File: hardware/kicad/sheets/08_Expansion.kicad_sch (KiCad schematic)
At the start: 0 parts

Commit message: Implement Package 09R expansion interface
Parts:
- added C1: 100 nF X7R ±10% local buffer decoupling, symbol IPC100:C
- added C2: 10 µF X7R accessory-bias reservoir; within ICD-00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, symbol IPC100:C
- added C3: 100 nF X7R ±10% core-side buffer decoupling, symbol IPC100:C
- added D1: J10 SDA low-capacitance TVS provision; IEC 61000-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, symbol IPC100:ESD_PROVISION
- added D2: J10 SCL low-capacitance TVS provision; IEC 61000-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, symbol IPC100:ESD_PROVISION
- added D3: EXPANSION_VCC local ESD/reverse-injection provisi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, symbol IPC100:ESD_PROVISION
- added FB1: Accessory-bias filter bead — impedance/current ra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, symbol IPC100:FERRITE
- added R1: 100 kΩ ±1% segment-enable fail-low bias, symbol IPC100:R
- added R2: 4.70 kΩ ±1% J10 SDA pull-up; Sheet 08 external-se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, symbol IPC100:R
- added R3: 4.70 kΩ ±1% J10 SCL pull-up; Sheet 08 external-se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, symbol IPC100:R
- added R4: 47 Ω J10 SDA series damping; final 33–100 Ω by SI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, symbol IPC100:R
- added R5: 47 Ω J10 SCL series damping; final 33–100 Ω by SI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, symbol IPC100:R
- added TP1: EXPANSION_VCC DFT, symbol IPC100:TEST_NODE
- added TP2: SEGMENT_ENABLE DFT, symbol IPC100:TEST_NODE
- added TP3: INTERNAL SDA DFT, symbol IPC100:TEST_NODE
- added TP4: INTERNAL SCL DFT, symbol IPC100:TEST_NODE
- added TP5: J10 SDA DFT, symbol IPC100:TEST_NODE
- added TP6: J10 SCL DFT, symbol IPC100:TEST_NODE
- added U1: 2.9 V assert / 2.7 V deassert rail qualifier; ≥5 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, symbol IPC100:EXPANSION_RAIL_QUALIFIER
- added U2: Dual-supply I2C hot-swap buffer; 100 kHz; fail-di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, symbol IPC100:I2C_SEGMENT_BUFFER
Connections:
- net +3V3_CORE: now also C3.2, U1.3 (GND)
- net EXPANSION_VCC: now also D3.1 (LINE), FB1.1 (IN), TP1.1 (NODE)
- net I2C_SCL: now also TP4.1 (NODE), U2.3 (SCL_INT)
- net I2C_SDA: now also TP3.1 (NODE)
- net J10_I2C_SCL: now also D2.1 (LINE), R5.1, TP6.1 (NODE)
- net J10_I2C_SDA: now also D1.1 (LINE), R4.1, TP5.1 (NODE)
- new net EXPANSION_SEGMENT_ENABLE: R1.2, TP2.1 (NODE), U1.4 (SEGMENT_ENABLE)
- new net EXPANSION_VCC_FILT: C1.2, C2.2, FB1.2 (OUT), R2.2, R3.2, U1.2 (EXP_VCC_SENSE), U2.8 (GND)
- new net EXP_SCL_BUFFERED: R3.1, R5.2, U2.7 (SCL_EXT)
- new net EXP_SDA_BUFFERED: R2.1, R4.2
- new net GND: C1.1, C2.1, C3.1, D1.2 (RETURN), D2.2 (RETURN), D3.2 (RETURN), R1.1, U1.1 (CORE_VDD), U2.5 (VCC_EXT)
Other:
- note added: "1 — OPTIONAL EXPANSION POWER FILTER / RAIL-VALID QUALIFICATION"
- note added: "2 — FAIL-DISABLED SEGMENTED I2C BUFFER (100 kHz; NO CLOCK STRETCHING)"
- note added: "3 — EXTERNAL-SIDE PULL-UPS, SERIES DAMPING & PROTECTION PROVISIONS"
- note added: "4 — SCHEMATIC DFT NODES (PHYSICAL PADS REMAIN SHEET 09 / PCB SCOPE)"
- note added: "Dual-supply hot-swap class: high-Z when disabled/unpowered, ≤10 µA powered-off leakage per line, no false-low startup pulse, external stuck-low isolated after disable. Sheet 07 remains sole internal pull-up owner."
- note added: "ICD-001 REV A RESTRICTIONS: DNP DEFAULT; ONE ACCESSORY; 0x30–0x37; NO CLOCK STRETCHING; NO CAN/RS-485/UART/SPI/USB/RANGEHUB; NO GPIO37; NON-SAFETY FIRMWARE DATA ONLY."
- note added: "One accessory, address 0x30–0x37, 0.30 m maximum, 100 pF segment maximum. Generic TVS provisions require final low-capacitance part/placement selection with Sheet 09; no connector or footprint is present."
- note added: "Probe power, rail-valid enable, both internal bus lines, and both isolated external lines. No footprint assignments are authorized."
- note added: "Sheet 02 remains sole switch/current-limit owner. Sheet 08 filters only its local external-side bias/logic supply and releases the segment at ≥2.9 V after 5 ms; disables by ≤2.7 V. Entire option DNP by default."
- note removed: "Detailed implementation intentionally deferred to subsequent engineering package."
- note removed: "PACKAGE 01 PLACEHOLDER — NO CIRCUITRY OR FOOTPRINTS"
- title: IPC-100 Rev A — 08 Expansion -> IPC-100 Rev A — 08 Restricted Expansion Interface

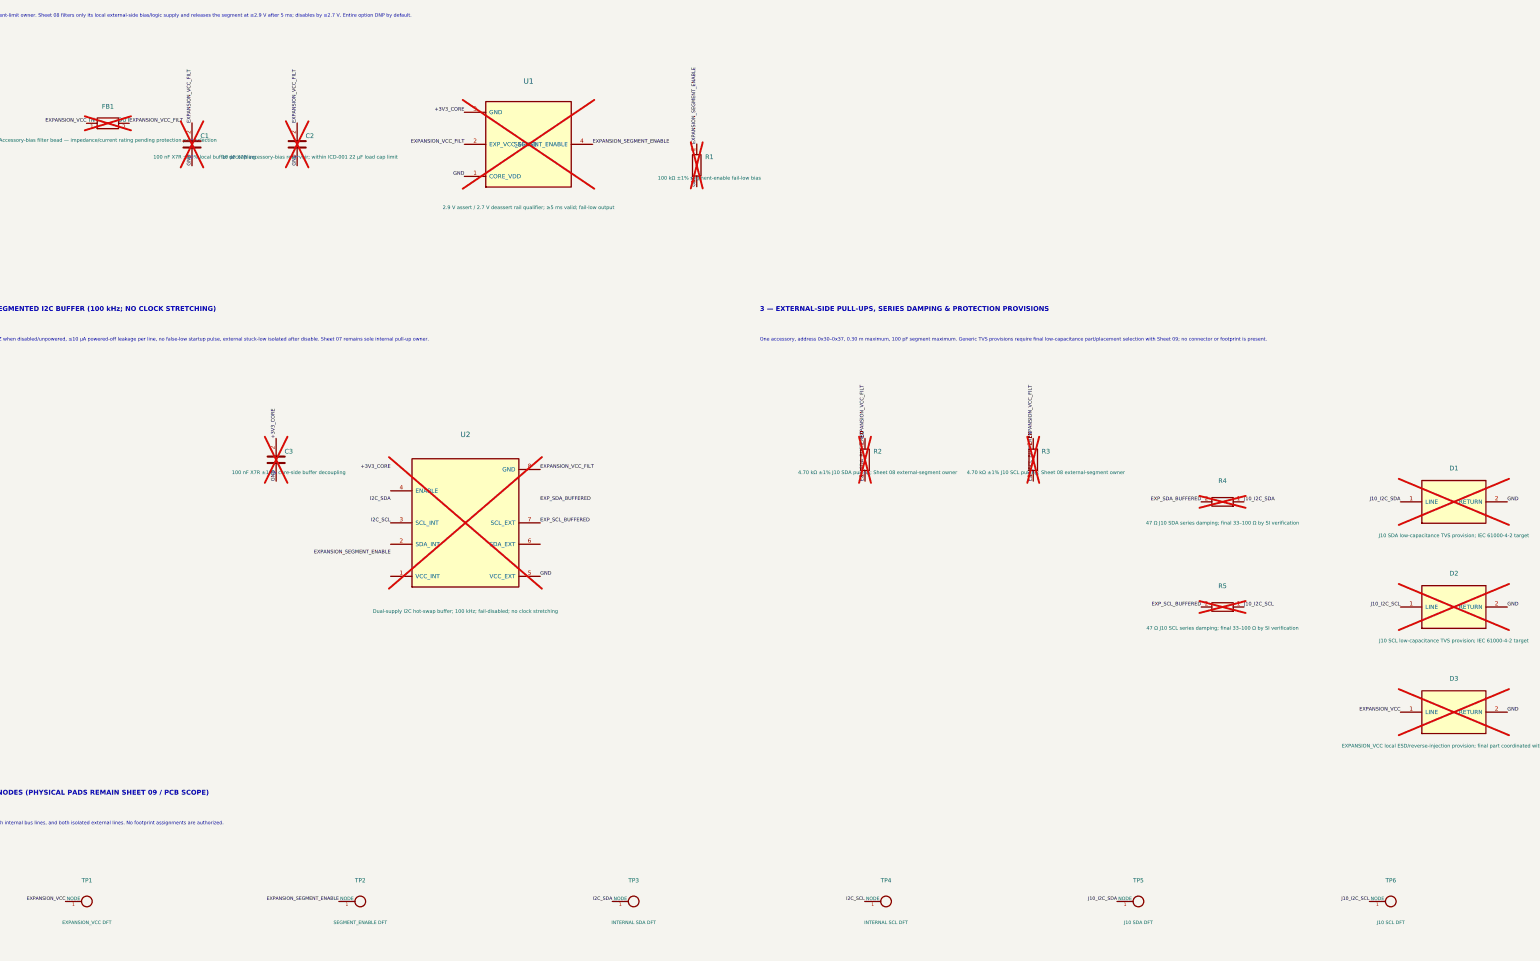
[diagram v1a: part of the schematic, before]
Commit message: Normalize Rev A reference designators
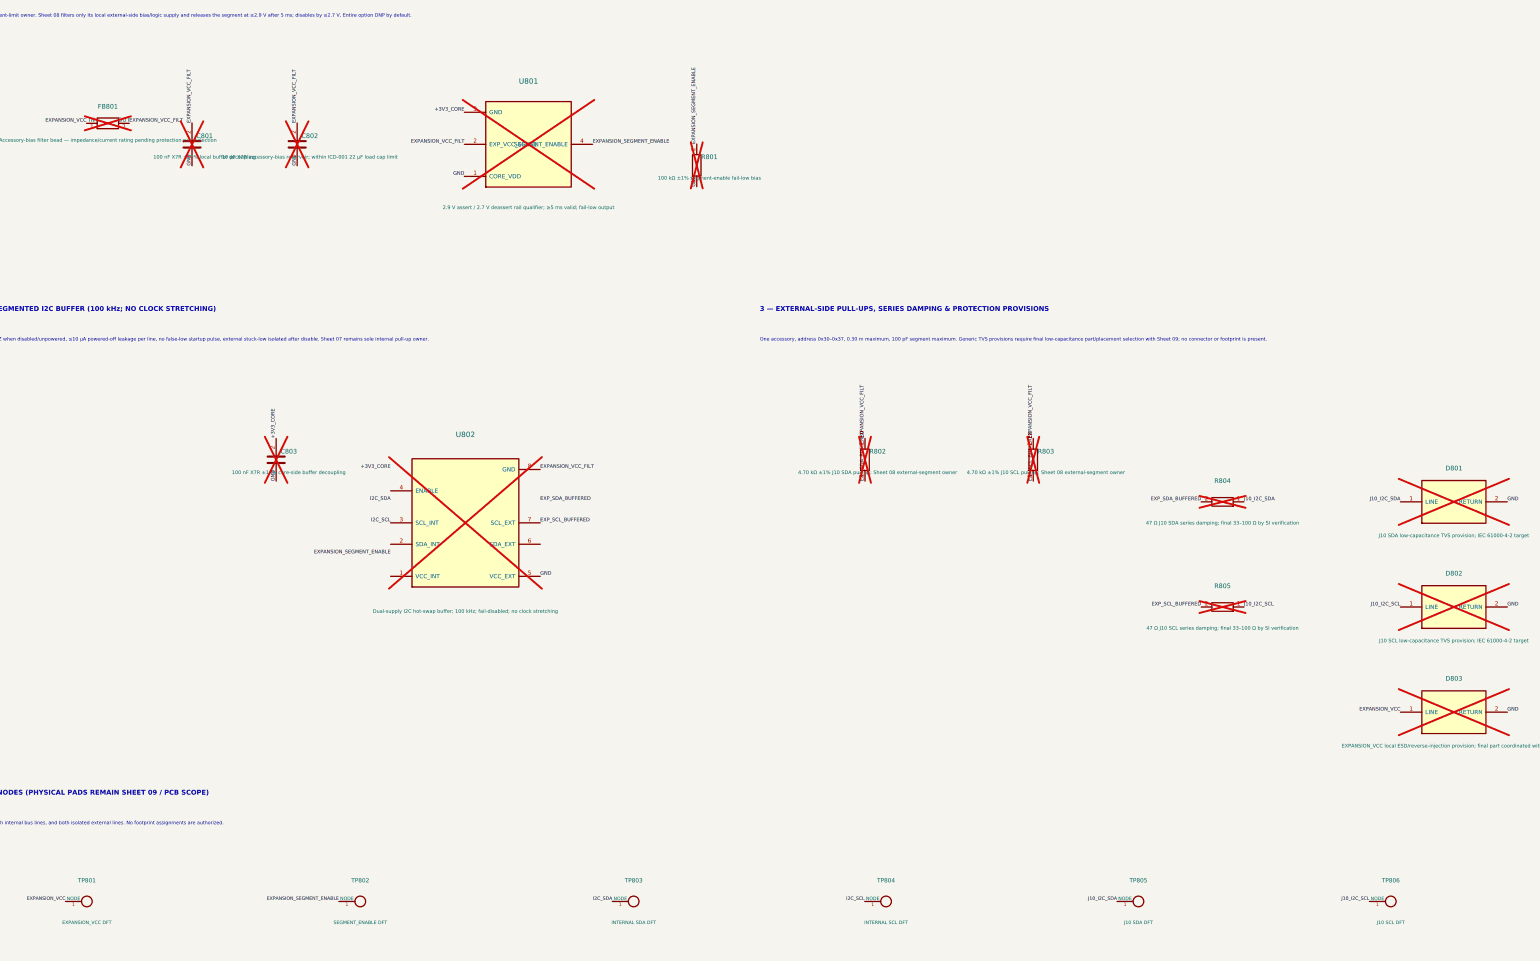
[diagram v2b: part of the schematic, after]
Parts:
- renumbered C1 to C801, C2 to C802, C3 to C803, D1 to D801, D2 to D802, D3 to D803, FB1 to FB801, R1 to R801, R2 to R802, R3 to R803, R4 to R804, R5 to R805, TP1 to TP801, TP2 to TP802, TP3 to TP803, TP4 to TP804, TP5 to TP805, TP6 to TP806, U1 to U801, U2 to U802

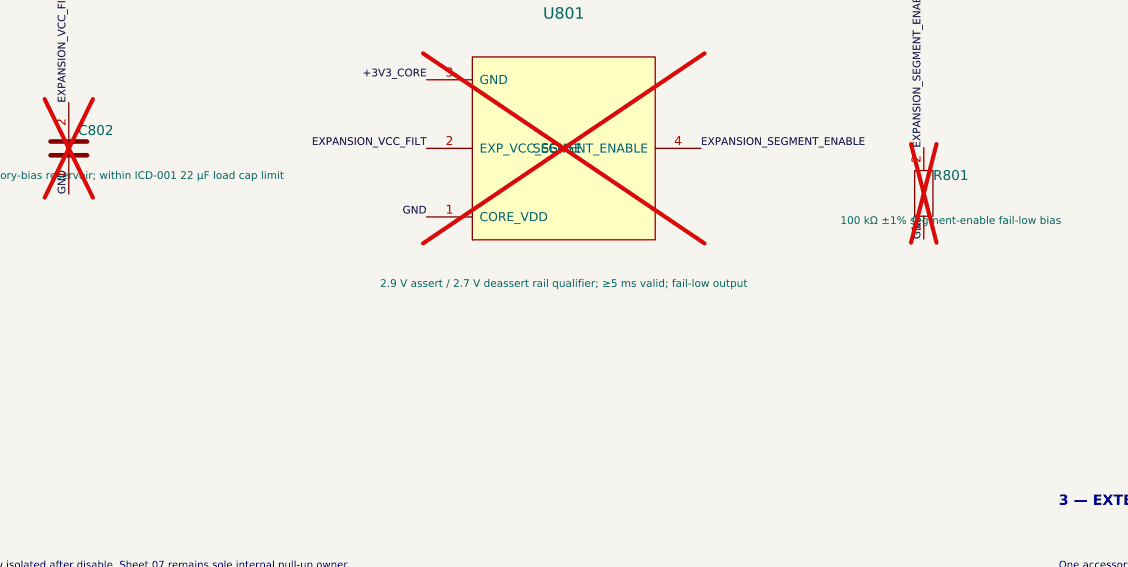
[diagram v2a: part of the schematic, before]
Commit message: Complete ECO-006 power compatibility remediation
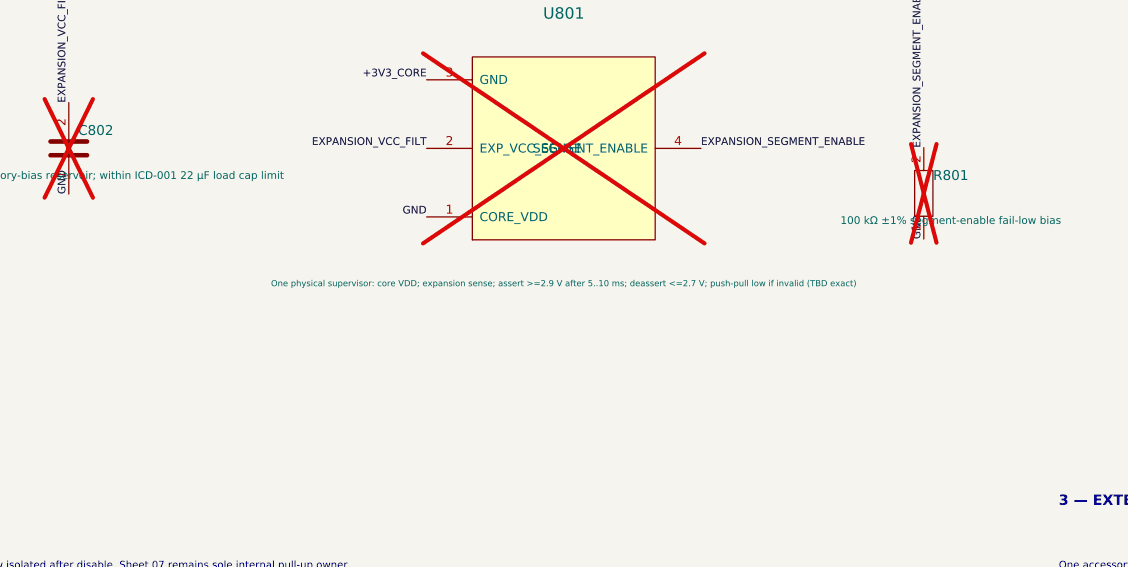
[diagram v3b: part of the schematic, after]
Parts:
- U801: value 2.9 V assert / 2.7 V deassert rail qualifier; ≥5 ms valid; fail-low output -> One physical supervisor: core VDD; expansion sense; assert >=2.9 V after 5..10 ms; deassert <=2.7 V; push-pull low if i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; symbol IPC100:EXPANSION_RAIL_QUALIFIER -> IPC100:RAIL_VALID_SUPERVISOR_PP
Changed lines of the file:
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@@
   (label "EXPANSION_VCC_FILT" (at 110 49.92 90) (effects (font (size 0.85 0.85)) (justify left bottom)))
   (label "GND" (at 110 60.08 90) (effects (font (size 0.85 0.85)) (justify left bottom)))
-  (symbol (lib_id "IPC100:EXPANSION_RAIL_QUALIFIER") (at 165 55 0) (unit 1) (exclude_from_sim no) (in_bom yes) (on_board yes) (dnp yes)
+  (symbol (lib_id "IPC100:RAIL_VALID_SUPERVISOR_PP") (at 165 55 0) (unit 1) (exclude_from_sim no) (in_bom yes) (on_board yes) (dnp yes)
     (property "Reference" "U801" (at 165 40 0) (effects (font (size 1.27 1.27))))
-    (property "Value" "2.9 V assert / 2.7 V deassert rail qualifier; ≥5 ms valid; fail-low output" (at 165 70 0) (effects (font (size 0.85 0.85))))
+    (property "Value" "One physical supervisor: core VDD; expansion sense; assert >=2.9 V after 5..10 ms; deassert <=2.7 V; push-pull low if invalid (TBD exact)" (at 165 70 0) (effects (font (size 0.68 0.68))))
     (property "Footprint" "" (at 165 55 0) (effects (font (size 1 1)) hide)) (property "Datasheet" "" (at 165 55 0) (effects (font (size 1 1)) hide))
     (pin "1") (pin "2")

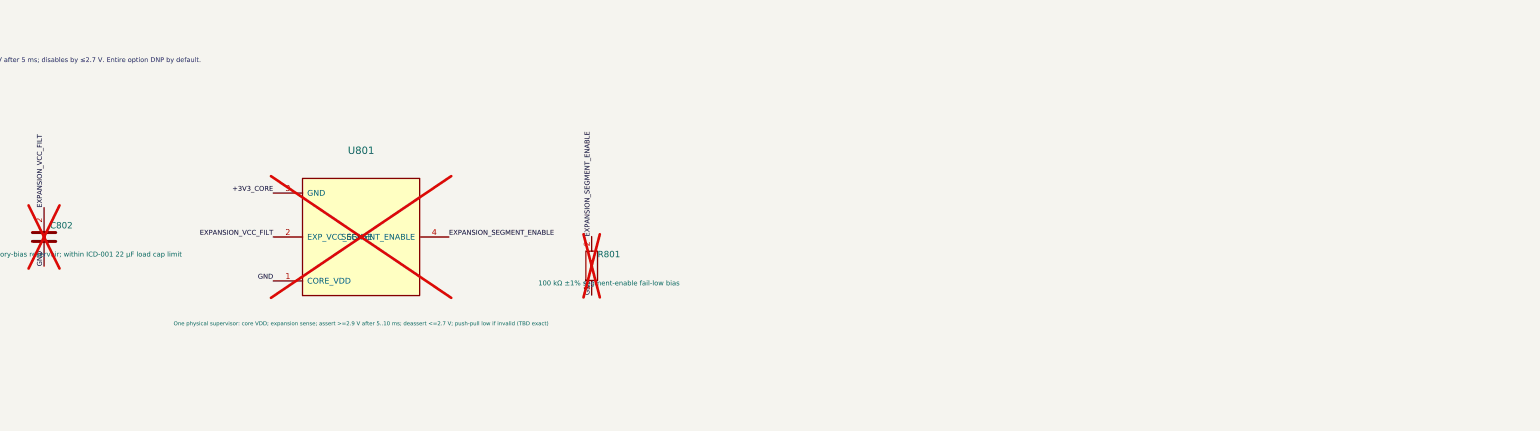
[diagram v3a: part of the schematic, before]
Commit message: Complete ECO-007 power programming corrections
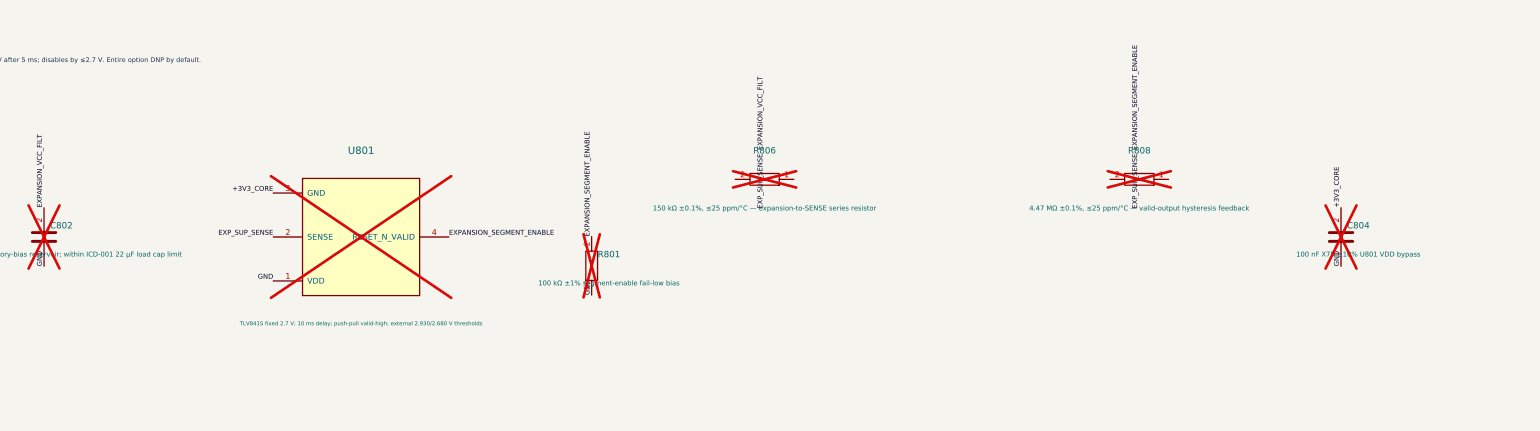
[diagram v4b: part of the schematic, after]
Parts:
- added C804: 100 nF X7R ±10% U801 VDD bypass, symbol IPC100:C
- added R806: 150 kΩ ±0.1%, ≤25 ppm/°C — expansion-to-SENSE ser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, symbol IPC100:R
- added R808: 4.47 MΩ ±0.1%, ≤25 ppm/°C — valid-output hysteres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, symbol IPC100:R
- U801: value One physical supervisor: core VDD; expansion sense; assert >=2.9 V after 5..10 ms; deassert <=2.7 V; push-pull low if i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 -> TLV841S fixed 2.7 V; 10 ms delay; push-pull valid-high; external 2.930/2.680 V thresholds; symbol IPC100:RAIL_VALID_SUPERVISOR_PP -> IPC100:TLV841S_2V7_VALID_HIGH
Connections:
- net +3V3_CORE: now also C804.2
- net EXPANSION_VCC_FILT: no longer U801.2 (EXP_VCC_SENSE)
- net GND: now also C804.1
- new net EXP_SUP_SENSE: U801.2 (SENSE)
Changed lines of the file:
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@@
   (label "EXPANSION_VCC_FILT" (at 110 49.92 90) (effects (font (size 0.85 0.85)) (justify left bottom)))
   (label "GND" (at 110 60.08 90) (effects (font (size 0.85 0.85)) (justify left bottom)))
-  (symbol (lib_id "IPC100:RAIL_VALID_SUPERVISOR_PP") (at 165 55 0) (unit 1) (exclude_from_sim no) (in_bom yes) (on_board yes) (dnp yes)
+  (symbol (lib_id "IPC100:TLV841S_2V7_VALID_HIGH") (at 165 55 0) (unit 1) (exclude_from_sim no) (in_bom yes) (on_board yes) (dnp yes)
     (property "Reference" "U801" (at 165 40 0) (effects (font (size 1.27 1.27))))
-    (property "Value" "One physical supervisor: core VDD; expansion sense; assert >=2.9 V after 5..10 ms; deassert <=2.7 V; push-pull low if invalid (TBD exact)" (at 165 70 0) (effects (font (size 0.68 0.68))))
-    (property "Footprint" "" (at 165 55 0) (effects (font (size 1 1)) hide)) (property "Datasheet" "" (at 165 55 0) (effects (font (size 1 1)) hide))
+    (property "Value" "TLV841S fixed 2.7 V; 10 ms delay; push-pull valid-high; external 2.930/2.680 V thresholds" (at 165 70 0) (effects (font (size 0.68 0.68))))
+    (property "Footprint" "" (at 165 55 0) (effects (font (size 1 1)) hide)) (property "Datasheet" "https://www.ti.com/lit/ds/symlink/tlv841.pdf" (at 165 55 0) (effects (font (size 1 1)) hide))
     (pin "1") (pin "2")
     (pin "3") (pin "4")
@@
   )
   (label "+3V3_CORE" (at 149.76 47.38 180) (effects (font (size 0.85 0.85)) (justify right bottom)))
-  (label "EXPANSION_VCC_FILT" (at 149.76 55 180) (effects (font (size 0.85 0.85)) (justify right bottom)))
+  (label "EXP_SUP_SENSE" (at 149.76 55 180) (effects (font (size 0.85 0.85)) (justify right bottom)))
   (label "GND" (at 149.76 62.62 180) (effects (font (size 0.85 0.85)) (justify right bottom)))
   (label "EXPANSION_SEGMENT_ENABLE" (at 180.24 55 0) (effects (font (size 0.85 0.85)) (justify left bottom)))
@@
   (label "EXPANSION_SEGMENT_ENABLE" (at 205 54.92 90) (effects (font (size 0.85 0.85)) (justify left bottom)))
   (label "GND" (at 205 65.08 90) (effects (font (size 0.85 0.85)) (justify left bottom)))
+  (symbol (lib_id "IPC100:R") (at 235 45 90) (unit 1) (exclude_from_sim no) (in_bom yes) (on_board yes) (dnp yes)
+    (property "Reference" "R806" (at 235 40 90) (effects (font (size 1.1 1.1))))
+    (property "Value" "150 kΩ ±0.1%, ≤25 ppm/°C — expansion-to-SENSE series resistor" (at 235 50 90) (effects (font (size 0.85 0.85))))
+    (property "Footprint" "" (at 235 45 0) (effects (font (size 1 1)) hide)) (property "Datasheet" "" (at 235 45 0) (effects (font (size 1 1)) hide))
+    (pin "1") (pin "2")
+    (instances (project "IPC-100" (path "/10000000-0000-4000-8000-000000000001/10000000-0000-4000-8000-000000000432" (reference "R806") (unit 1))))
+  )
+  (label "EXPANSION_VCC_FILT" (at 235 39.92 90) (effects (font (size 0.85 0.85)) (justify left bottom)))
+  (label "EXP_SUP_SENSE" (at 235 50.08 90) (effects (font (size 0.85 0.85)) (justify left bottom)))
+  (symbol (lib_id "IPC100:R") (at 300 45 90) (unit 1) (exclude_from_sim no) (in_bom yes) (on_board yes) (dnp yes)
+    (property "Reference" "R808" (at 300 40 90) (effects (font (size 1.1 1.1))))
+    (property "Value" "4.47 MΩ ±0.1%, ≤25 ppm/°C — valid-output hysteresis feedback" (at 300 50 90) (effects (font (size 0.85 0.85))))
+    (property "Footprint" "" (at 300 45 0) (effects (font (size 1 1)) hide)) (property "Datasheet" "" (at 300 45 0) (effects (font (size 1 1)) hide))
+    (pin "1") (pin "2")
+    (instances (project "IPC-100" (path "/10000000-0000-4000-8000-000000000001/10000000-0000-4000-8000-000000000432" (reference "R808") (unit 1))))
+  )
+  (label "EXPANSION_SEGMENT_ENABLE" (at 300 39.92 90) (effects (font (size 0.85 0.85)) (justify left bottom)))
+  (label "EXP_SUP_SENSE" (at 300 50.08 90) (effects (font (size 0.85 0.85)) (justify left bottom)))
+  (symbol (lib_id "IPC100:C") (at 335 55 0) (unit 1) (exclude_from_sim no) (in_bom yes) (on_board yes) (dnp yes)
+    (property "Reference" "C804" (at 338 53 0) (effects (font (size 1.1 1.1))))
+    (property "Value" "100 nF X7R ±10% U801 VDD bypass" (at 338 58 0) (effects (font (size 0.85 0.85))))
+    (property "Footprint" "" (at 335 55 0) (effects (font (size 1 1)) hide)) (property "Datasheet" "" (at 335 55 0) (effects (font (size 1 1)) hide))
+    (pin "1") (pin "2")
+    (instances (project "IPC-100" (path "/10000000-0000-4000-8000-000000000001/10000000-0000-4000-8000-000000000432" (reference "C804") (unit 1))))
+  )
+  (label "+3V3_CORE" (at 335 49.92 90) (effects (font (size 0.85 0.85)) (justify left bottom)))
+  (label "GND" (at 335 60.08 90) (effects (font (size 0.85 0.85)) (justify left bottom)))
   (text "2 — FAIL-DISABLED SEGMENTED I2C BUFFER (100 kHz; NO CLOCK STRETCHING)" (at 20 95 0) (effects (font (size 1.15 1.15) (bold yes)) (justify left bottom)))
   (text "Dual-supply hot-swap class: high-Z when disabled/unpowered, ≤10 µA powered-off leakage per line, no false-low startup pulse, external stuck-low isolated after disable. Sheet 07 remains sole internal pull-up owner." (at 20 102 0) (effects (font (size 0.82 0.82)) (justify left bottom)))
